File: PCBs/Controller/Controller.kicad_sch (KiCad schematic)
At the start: 10 parts, among them J1 RJ45, J2 RJ45, J3 RJ45, J4 RJ45, J5 Barrel_Jack_Switch, J6 Conn_01x04_Pin, SW1 RotaryEncoder_Switch_MP, U1 Pico, U2 AMS1117-3.3

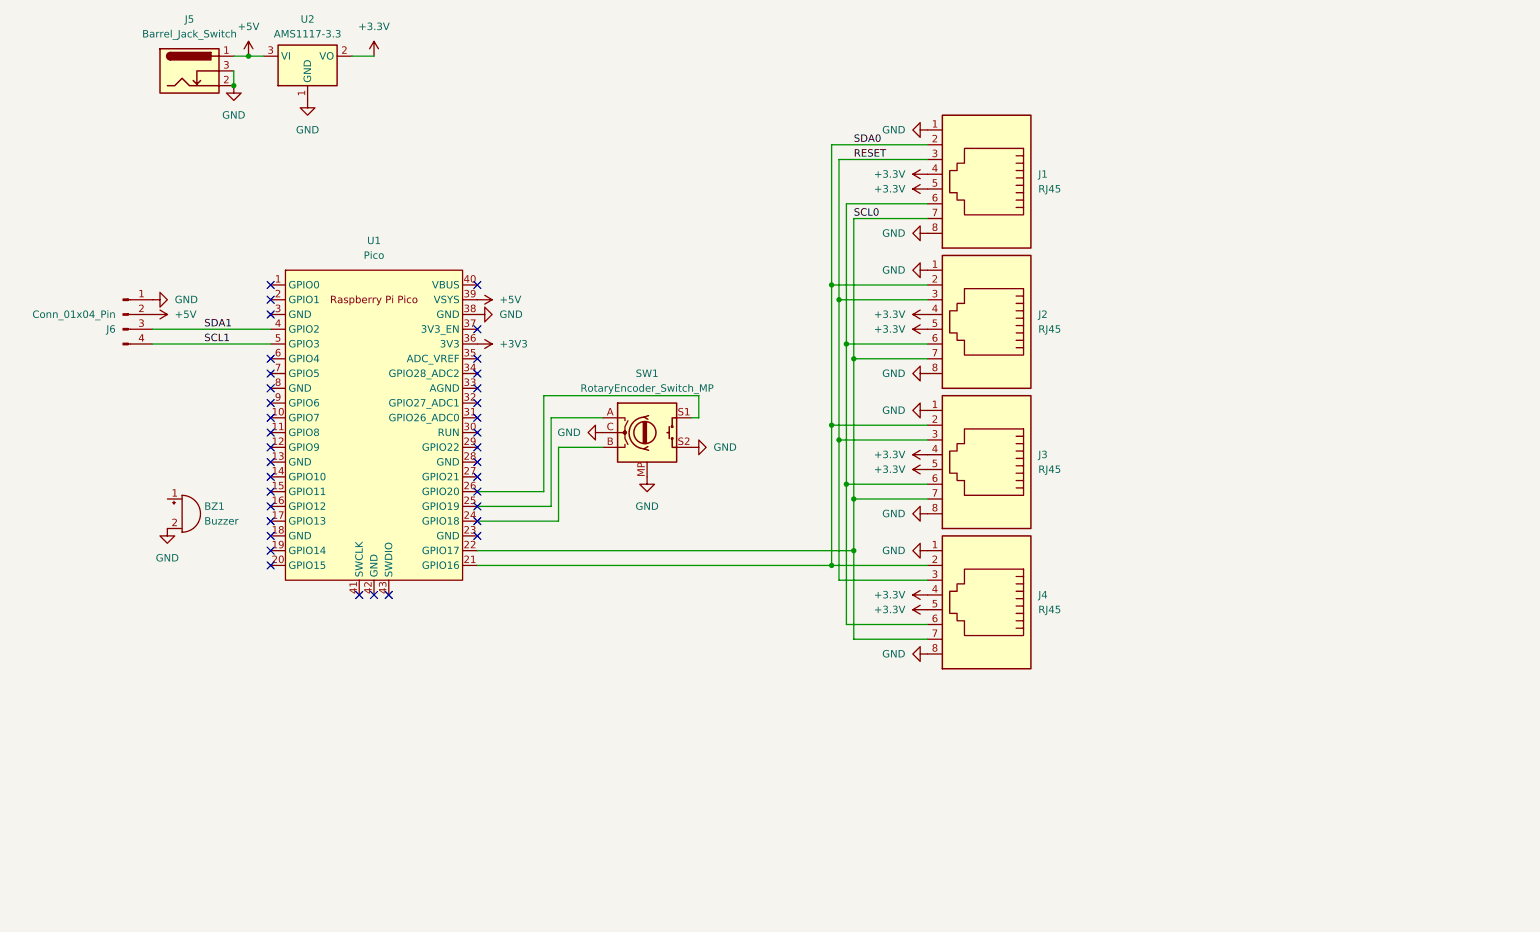
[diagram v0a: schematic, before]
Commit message: update RJ45 pins and pwr_flag
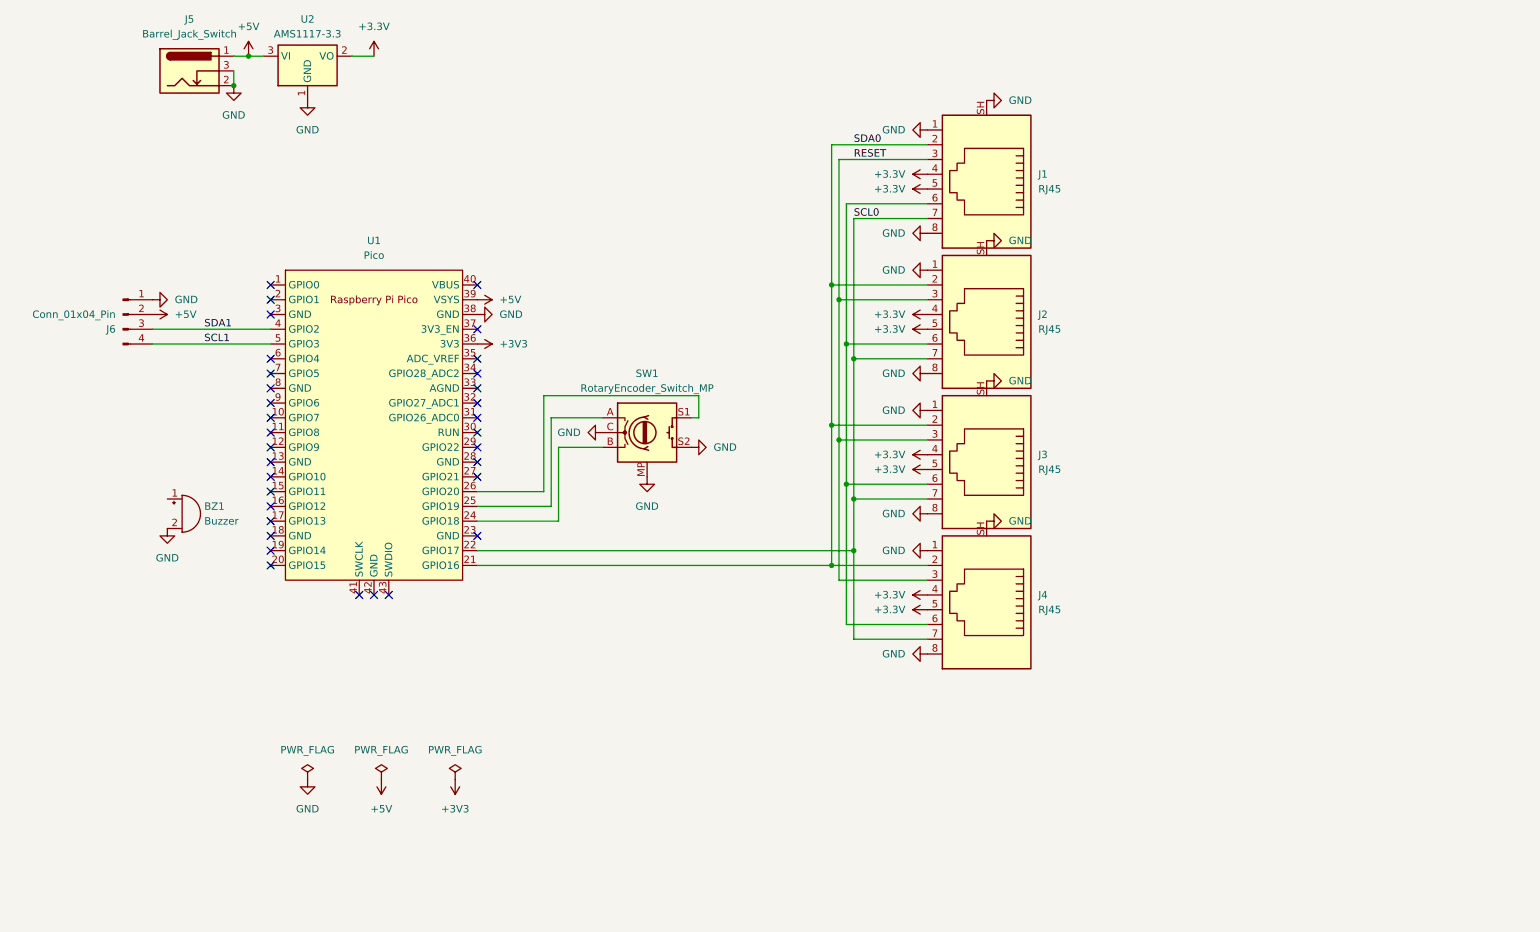
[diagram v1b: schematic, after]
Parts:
- J1, J2, J3, J4: symbol Connector:RJ45 -> Connector:RJ45_Shielded
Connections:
- net GND: now also J1.SH, J2.SH, J3.SH, J4.SH
- no-connect marks 36 -> 33

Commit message: update sensor
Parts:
- added J7: Conn_01x03_Pin, Connector_PinHeader_2.54mm:PinHeader_1x03_P2.54mm_Vertical, symbol Connector:Conn_01x03_Pin
- added JP1: Jumper_2_Open, Jumper:SolderJumper-2_P1.3mm_Open_RoundedPad1.0x1.5mm, symbol Jumper:Jumper_2_Open
- added JP2: Jumper_3_Bridged12, Jumper:SolderJumper-3_P1.3mm_Bridged12_RoundedPad1.0x1.5mm, symbol Jumper:Jumper_3_Bridged12
- added JP3: Jumper_2_Bridged, Jumper:SolderJumper-2_P1.3mm_Bridged_RoundedPad1.0x1.5mm, symbol Jumper:Jumper_2_Bridged
- added SW2: SW_Push, Button_Switch_THT:SW_PUSH_6mm_H4.3mm, symbol Switch:SW_Push
- SW1: value RotaryEncoder_Switch_MP -> RotaryEncoder_Switch; symbol Device:RotaryEncoder_Switch_MP -> Device:RotaryEncoder_Switch
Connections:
- net +3.3V: now also JP2.2 (C); no longer U2.2 (VO)
- net +3V3: now also JP2.3 (B)
- net GND: now also SW1.S1, U1.13 (GND), U1.18 (GND), U1.23 (GND), U1.28 (GND), U1.3 (GND), U1.42 (GND), U1.8 (GND), J7.2 (Pin_2), SW2.1; no longer SW1.MP, SW1.S2
- net SCL1: now also U1.20 (GPIO15); no longer U1.5 (GPIO3)
- net SDA1: now also U1.19 (GPIO14); no longer U1.4 (GPIO2)
- net BZ1: now reaches BZ1.1 (+)
- net BZ1: now also U1.27 (GPIO21)
- net at J1.6, J2.6, J3.6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: now also JP1.2 (B)
- net RE_A: now reaches U1.15 (GPIO11)
- net RE_A: now also SW1.A
- net RE_S: now reaches U1.16 (GPIO12)
- net RE_S: now also SW1.S2
- net RE_B: now reaches U1.17 (GPIO13)
- net RE_B: now also SW1.B
- net AT_RS: now reaches U1.24 (GPIO18)
- net AT_RS: now also JP3.1 (A); no longer SW1.B
- net FU: now reaches U1.25 (GPIO19)
- net FU: now also JP1.1 (A); no longer SW1.A
- net at U1.26 (GPIO20): no longer SW1.S1
- net RUN: now reaches U1.30 (RUN)
- net RUN: now also SW2.2
- net at U1.41 (SWCLK): now also J7.1 (Pin_1)
- net at U1.43 (SWDIO): now also J7.3 (Pin_3)
- net RESET: no longer names the net of J1.3, J2.3, J3.3, J4.3
- net RESET: now also JP3.2 (B)
- new net: JP2.1 (A), U2.2 (VO)
- no-connect marks 33 -> 19
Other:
- moved on the sheet: BZ1, J1, J2, J3, J4, J6

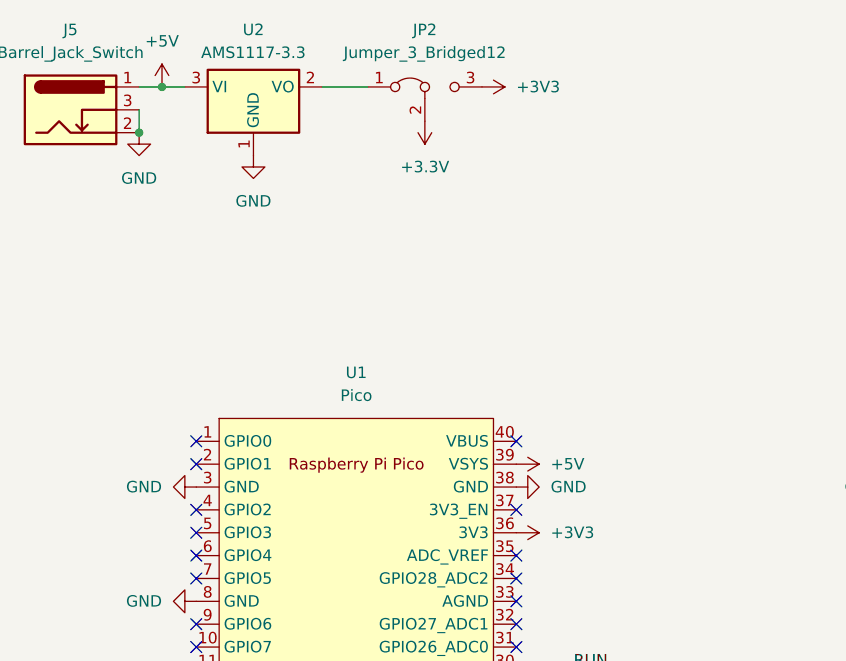
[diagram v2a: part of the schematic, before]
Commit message: added Capacitors
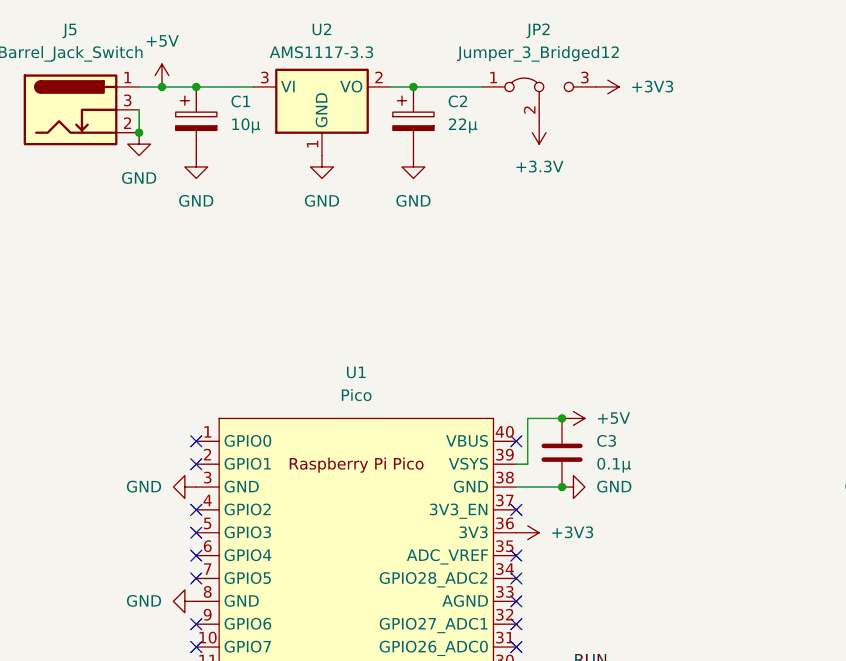
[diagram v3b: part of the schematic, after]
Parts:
- added C1: 10μ, Capacitor_THT:CP_Radial_D5.0mm_P2.00mm, symbol Device:C_Polarized
- added C2: 22μ, Capacitor_THT:CP_Radial_D5.0mm_P2.00mm, symbol Device:C_Polarized
- added C3: 0.1μ, Capacitor_THT:C_Disc_D3.0mm_W1.6mm_P2.50mm, symbol Device:C
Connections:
- net +5V: now also C1.1, C3.1
- net GND: now also C1.2, C2.2, C3.2
- net at JP2.1 (A), U2.2 (VO): now also C2.1
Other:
- moved on the sheet: JP2, U2

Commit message: Controller Rev. 01
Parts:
- removed C2: 22μ, Capacitor_THT:CP_Radial_D5.0mm_P2.00mm, symbol Device:C_Polarized
- removed J7: Conn_01x03_Pin, Connector_PinHeader_2.54mm:PinHeader_1x03_P2.54mm_Vertical, symbol Connector:Conn_01x03_Pin
- removed JP2: Jumper_3_Bridged12, Jumper:SolderJumper-3_P1.3mm_Bridged12_RoundedPad1.0x1.5mm, symbol Jumper:Jumper_3_Bridged12
- removed JP3: Jumper_2_Bridged, Jumper:SolderJumper-2_P1.3mm_Bridged_RoundedPad1.0x1.5mm, symbol Jumper:Jumper_2_Bridged
- removed U2: AMS1117-3.3, Package_TO_SOT_SMD:SOT-223-3_TabPin2, symbol Regulator_Linear:AMS1117-3.3
- added D1: LED_RKGB, LED_THT:LED_D5.0mm-4_RGB_Wide_Pins, symbol Device:LED_RKGB
- added JP1: Jumper_2_Open, Jumper:SolderJumper-2_P1.3mm_Open_RoundedPad1.0x1.5mm, symbol Jumper:Jumper_2_Open
- added R1, R2: 220, Resistor_THT:R_Axial_DIN0207_L6.3mm_D2.5mm_P10.16mm_Horizontal, symbol Device:R
- added R3: 110, Resistor_THT:R_Axial_DIN0207_L6.3mm_D2.5mm_P10.16mm_Horizontal, symbol Device:R
- added R4, R5: 10k, Resistor_THT:R_Axial_DIN0207_L6.3mm_D2.5mm_P10.16mm_Horizontal, symbol Device:R
- added R6: 5k, Resistor_THT:R_Axial_DIN0207_L6.3mm_D2.5mm_P10.16mm_Horizontal, symbol Device:R
- added U3: Level Converter, Library:Level_Converter, symbol Level_Converter:Level_Converter
- renumbered JP1 to JP2
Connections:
- net +3.3V is gone; now on net +5V: J1.4, J1.5, J2.4, J2.5, J3.4, J3.5, J4.4, J4.5
- net +3V3: now also U3.3 (LV)
- net +5V: now also R6.1, U3.9 (HV)
- net AT_RS: now also JP1.1 (A), U3.8 (HV2); no longer U1.24 (GPIO18)
- net BZ1: now also U1.7 (GPIO5); no longer U1.27 (GPIO21)
- net FU: now also R6.2, U3.7 (HV1); no longer U1.25 (GPIO19)
- net GND: now also D1.2 (K), R4.1, R5.2, U3.10 (GND), U3.4 (GND)
- net RE_A: now also R4.2
- net RE_B: now also R5.1
- net SCL0: now also U3.11 (HV3); no longer U1.22 (GPIO17)
- net SDA0: now also U3.12 (HV4); no longer U1.21 (GPIO16)
- net at J1.3, J2.3, J3.3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: now also JP1.2 (B)
- net RED: now reaches U1.10 (GPIO7)
- net RED: now also R1.2
- net GREEN: now reaches U1.11 (GPIO8)
- net GREEN: now also R2.2
- net BLUE: now reaches U1.12 (GPIO9)
- net BLUE: now also R3.2
- new net: D1.1 (RA), R1.1
- new net: D1.3 (GA), R2.1
- new net: D1.4 (BA), R3.1
- new net: U1.25 (GPIO19), U3.1 (LV1)
- new net: U1.24 (GPIO18), U3.2 (LV2)
- new net: U1.22 (GPIO17), U3.5 (LV3)
- new net: U1.21 (GPIO16), U3.6 (LV4)
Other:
- moved on the sheet: SW1

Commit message: Controller Rev. 02
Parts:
- removed C3: 0.1μ, Capacitor_THT:C_Disc_D3.0mm_W1.6mm_P2.50mm, symbol Device:C
- added D2: 1N4007, Diode_THT:D_DO-41_SOD81_P7.62mm_Horizontal, symbol Device:D_Schottky
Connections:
- net +3V3: now also R4.1, R5.1
- net +5V: now also D2.2 (A); no longer U1.39 (VSYS)
- net GND: no longer R4.1, R5.2
- net RE_B: now also R5.2; no longer R5.1
- new net: D2.1 (K), U1.39 (VSYS)
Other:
- moved on the sheet: R4, R5
